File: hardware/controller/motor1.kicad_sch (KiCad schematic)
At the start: 58 parts, among them Q2 NMOS, Q3 NMOS, Q4 NMOS, Q5 NMOS, Q6 NMOS, Q7 NMOS, U10 LM2105D, U11 LM2105D, U12 LMV331, U13 LMV331, U14 LMV331, U9 LM2105D

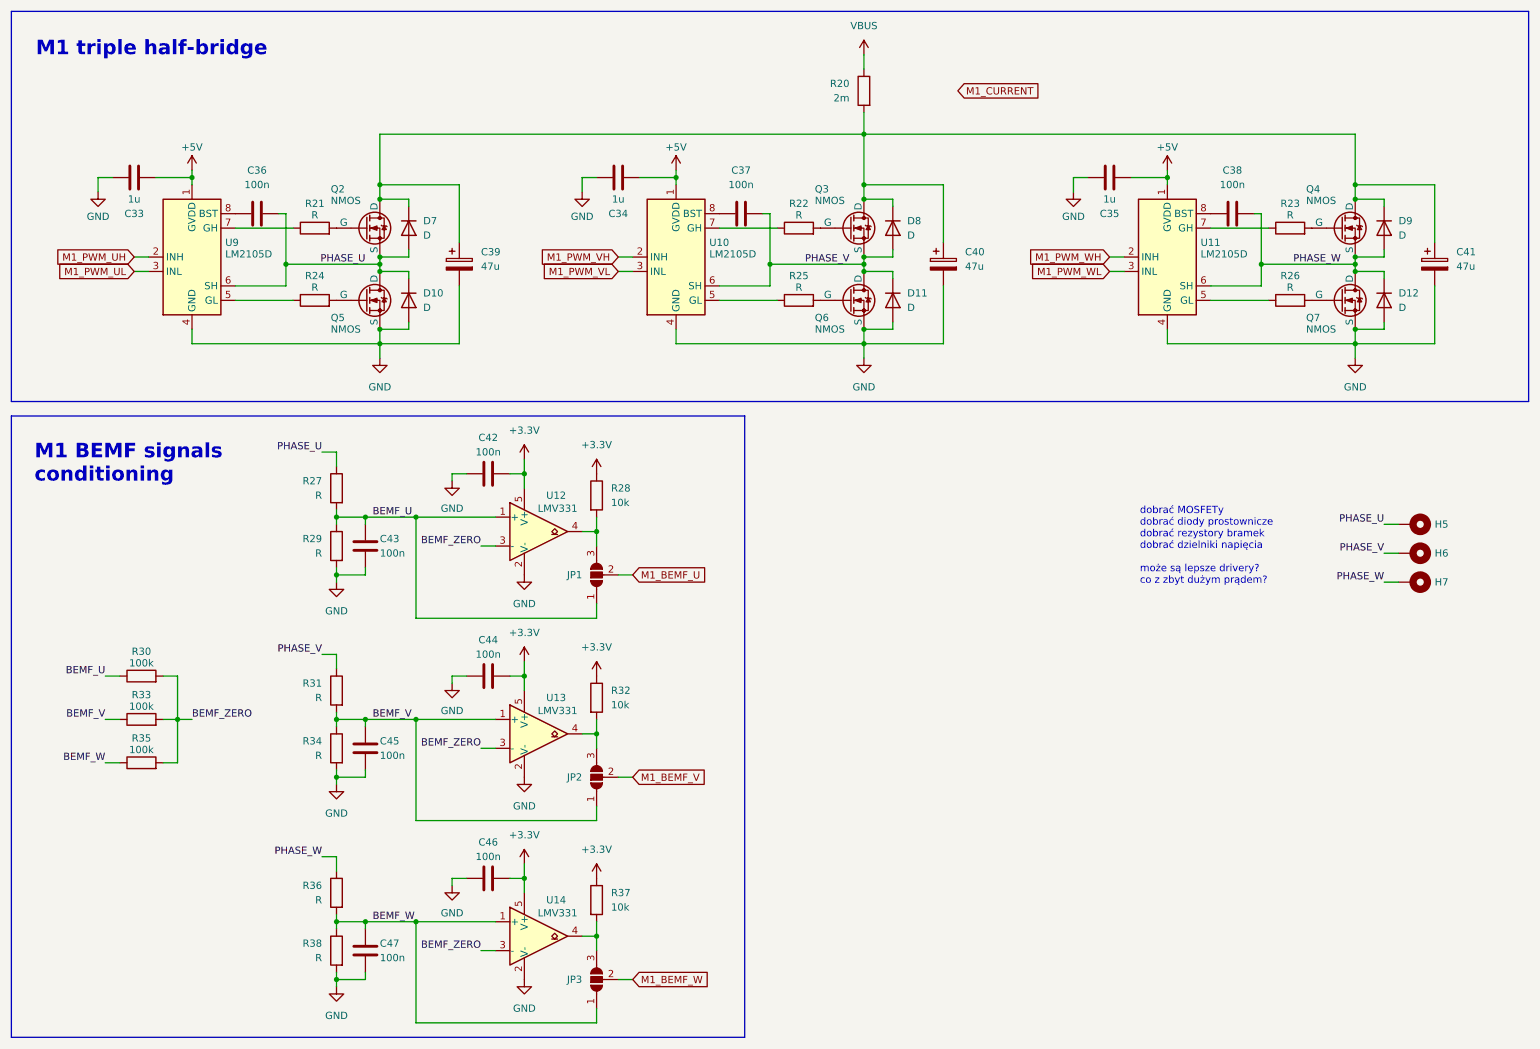
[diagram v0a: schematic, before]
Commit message: remove current sensing, external MOSFET diodes, BEMF filteringadd MOSFETs
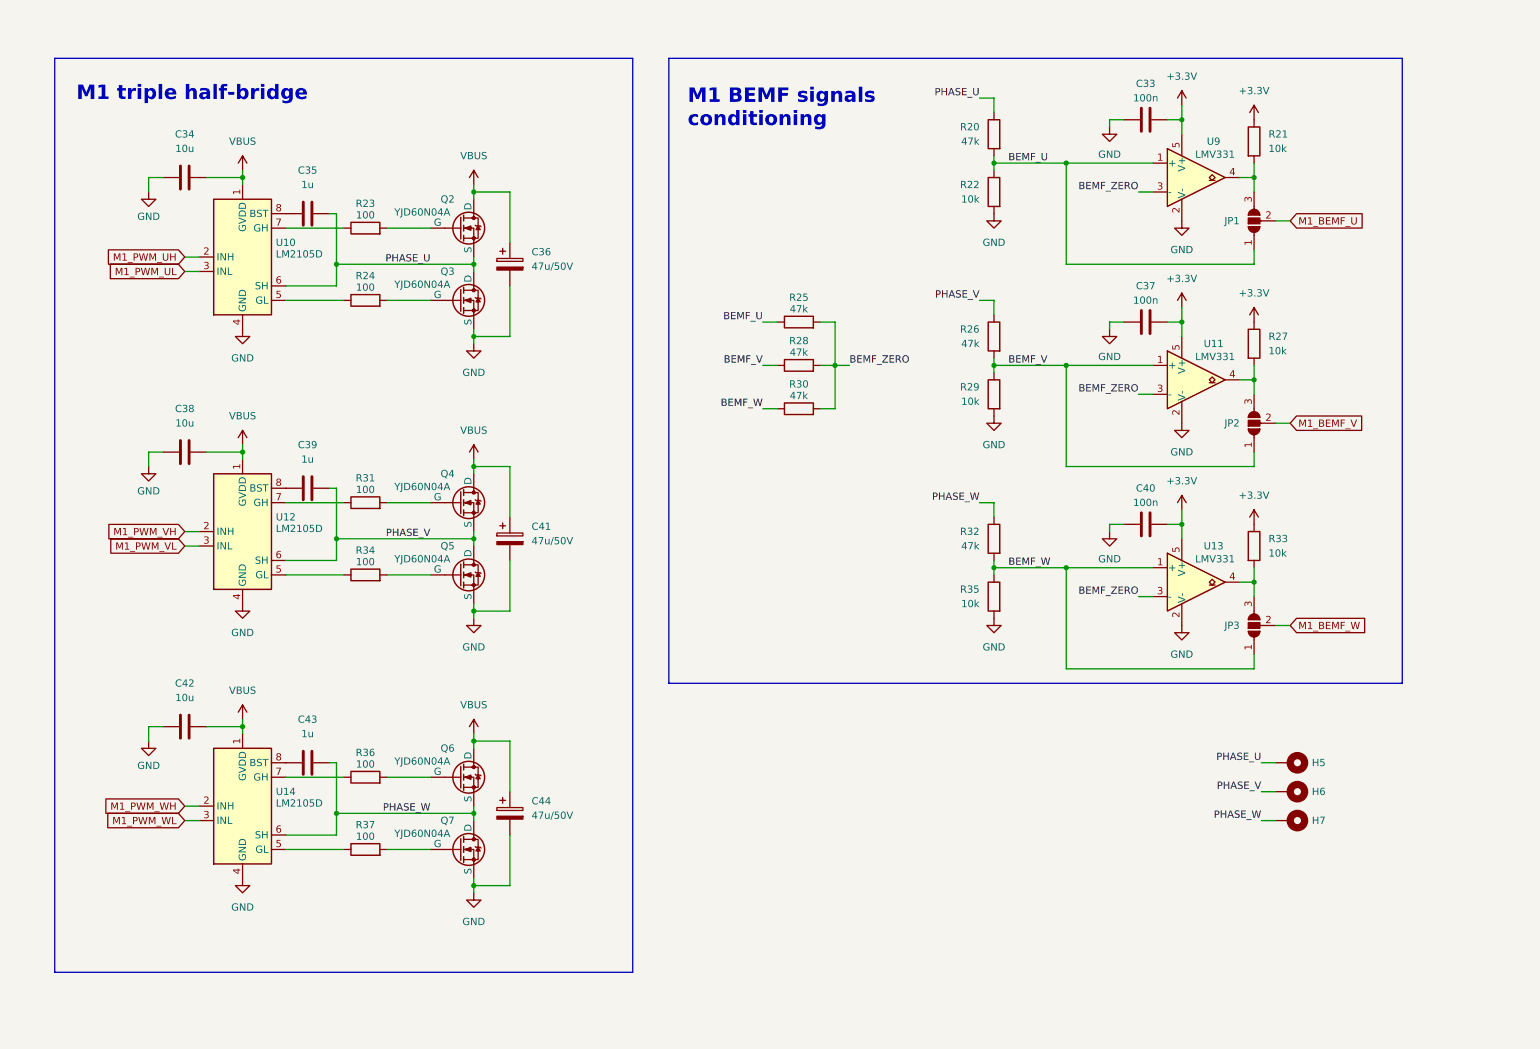
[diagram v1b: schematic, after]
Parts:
- removed C33, C35: 1u, symbol Device:C
- removed C37, C45, C47: 100n, symbol Device:C
- removed D10, D11, D12, D7, D8, D9: D, symbol Device:D
- removed R23, R25, R27: R, symbol Device:R
- added C39: 1u, symbol Device:C
- added C42: 10u, symbol Device:C
- added R36, R37: 100, symbol Device:R
- C34: value 1u -> 10u
- C35: renamed from C36; value 100n -> 1u
- C36: renamed from C39; value 47u -> 47u/50V
- C38: value 100n -> 10u
- C41: renamed from C40; value 47u -> 47u/50V
- C43: value 100n -> 1u
- C44: renamed from C41; value 47u -> 47u/50V
- Q2, Q3, Q4, Q5, Q6, Q7: value NMOS -> YJD60N04A
- R20: value 2m -> 47k
- R22, R29: value R -> 10k
- R23: renamed from R21; value R -> 100
- R24, R31, R34: value R -> 100
- R25: renamed from R30; value 100k -> 47k
- R26: value R -> 47k
- R28: renamed from R33; value 100k -> 47k
- R30: renamed from R35; value 100k -> 47k
- R32: renamed from R36; value R -> 47k
- R35: renamed from R38; value R -> 10k
- renumbered C42 to C33, C44 to C37, C46 to C40, R28 to R21, R32 to R27, R37 to R33, U9 to U10, U13 to U11, U10 to U12, U14 to U13, U11 to U14, U12 to U9
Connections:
- net BEMF_U: now also R20.2, R22.1; no longer C43.1, R29.1
- net BEMF_V: now also R26.2, R29.1; no longer R31.2, R34.1
- net GND: now also C34.1, C38.1, Q3.3 (S), R22.2, C42.1; no longer C34.2, C43.2, Q6.3 (S), R34.2
- net PHASE_U: now also Q3.1 (D), R20.1; no longer Q5.1 (D)
- net PHASE_V: now also Q4.3 (S), Q5.1 (D), R26.1, C39.2; no longer Q3.3 (S), Q6.1 (D), R31.1
- net PHASE_W: now also C43.2, Q6.3 (S); no longer C38.2, Q4.3 (S)
- net VBUS: now also C34.2, C36.1, C38.2, C41.1, C44.1, Q2.1 (D), Q4.1 (D), Q6.1 (D), U10.1 (GVDD), U12.1 (GVDD), U14.1 (GVDD), C42.2; no longer R20.1
- net at Q7.2 (G): now also R37.2; no longer R26.2
- net at U14.5 (GL): now also R37.1; no longer R26.1
- net at U14.7 (GH): now also R36.1
- net at U14.8 (BST): now also C43.1; no longer C38.1
- net at U12.5 (GL): now also R34.1
- net at U12.7 (GH): now also R31.1; no longer R22.1
- net at U12.8 (BST): now also C39.1
- net at Q3.2 (G): now also R24.2; no longer R22.2
- net at Q6.2 (G): now also R36.2
- net at Q5.2 (G): now also R34.2; no longer R24.2
- net at Q4.2 (G): now also R31.2
- removed net +5V: C34.1, U10.1 (GVDD), U12.1 (GVDD), U14.1 (GVDD)
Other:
- note removed: "dobrać MOSFETy dobrać diody prostownicze dobrać rezystory bramek dobrać dzielniki napięcia może są lepsze drivery? co z zbyt dużym prądem?"
- moved on the sheet: C33, C35, C36, C37, C40, C41, C44, H5, H6, H7, JP1, JP2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
